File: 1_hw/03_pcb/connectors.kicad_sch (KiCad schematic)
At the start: 0 parts

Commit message: FEAT: Added FTDI JTAG. Added 0 Ohm JTAG Resistors. Added Boot Select Switches.
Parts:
- added R? (x8): 0, Resistor_SMD:R_0603_1608Metric, symbol Device:R_Small
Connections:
- new net JTAG_CON_TCK_3P3: R?.2
- new net JTAG_CON_TDI_3P3: R?.2
- new net JTAG_CON_TDO_3P3: R?.2
- new net JTAG_CON_TMS_3P3: R?.2
- new net JTAG_FTDI_TCK_3P3: R?.2
- new net JTAG_FTDI_TDI_3P3: R?.2
- new net JTAG_FTDI_TDO_3P3: R?.2
- new net JTAG_FTDI_TMS_3P3: R?.2
- new net JTAG_MCU_TCK_3P3: R?.1, R?.1
- new net JTAG_MCU_TDI_3P3: R?.1, R?.1
- new net JTAG_MCU_TDO_3P3: R?.1, R?.1
- new net JTAG_MCU_TMS_3P3: R?.1, R?.1
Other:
- note added: "JTAG 0 OHM CONNECTIONS"

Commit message: FEAT: Simulated Analog Paths, added first stage analog amp to schematic.
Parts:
- R? (x8): symbol Device:R_Small -> Device:R_Small_US
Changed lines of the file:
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@@
 		(rev "0.0.1")
 		(company "Tomasz Brzyzek")
-		(comment 1 "Stasia Brzyzek")
 	)
 	(junction
@@
 	)
 	(symbol
-		(lib_id "Device:R_Small")
+		(lib_id "Device:R_Small_US")
 		(at 229.87 130.81 270)
 		(unit 1)
@@
 			)
 		)
-		(property "Description" ""
+		(property "Description" "Resistor, small US symbol"
 			(at 229.87 130.81 0)
 			(effects
@@
 	)
 	(symbol
-		(lib_id "Device:R_Small")
+		(lib_id "Device:R_Small_US")
 		(at 229.87 111.76 270)
 		(unit 1)
@@
 			)
 		)
-		(property "Description" ""
+		(property "Description" "Resistor, small US symbol"
 			(at 229.87 111.76 0)
 			(effects
@@
 	)
 	(symbol
-		(lib_id "Device:R_Small")
+		(lib_id "Device:R_Small_US")
 		(at 229.87 142.24 270)
 		(unit 1)
@@
 			)
 		)
-		(property "Description" ""
+		(property "Description" "Resistor, small US symbol"
 			(at 229.87 142.24 0)
 			(effects
@@
 	)
 	(symbol
-		(lib_id "Device:R_Small")
+		(lib_id "Device:R_Small_US")
 		(at 229.87 167.64 270)
 		(unit 1)
@@
 			)
 		)
-		(property "Description" ""
+		(property "Description" "Resistor, small US symbol"
 			(at 229.87 167.64 0)
 			(effects
@@
 	)
 	(symbol
-		(lib_id "Device:R_Small")
+		(lib_id "Device:R_Small_US")
 		(at 229.87 149.86 270)
 		(unit 1)
@@
 			)
 		)
-		(property "Description" ""
+		(property "Description" "Resistor, small US symbol"
 			(at 229.87 149.86 0)
 			(effects
@@
 	)
 	(symbol
-		(lib_id "Device:R_Small")
+		(lib_id "Device:R_Small_US")
 		(at 229.87 160.02 270)
 		(unit 1)
@@
 			)
 		)
-		(property "Description" ""
+		(property "Description" "Resistor, small US symbol"
 			(at 229.87 160.02 0)
 			(effects
@@
 	)
 	(symbol
-		(lib_id "Device:R_Small")
+		(lib_id "Device:R_Small_US")
 		(at 229.87 123.19 270)
 		(unit 1)
@@
 			)
 		)
-		(property "Description" ""
+		(property "Description" "Resistor, small US symbol"
 			(at 229.87 123.19 0)
 			(effects
@@
 	)
 	(symbol
-		(lib_id "Device:R_Small")
+		(lib_id "Device:R_Small_US")
 		(at 229.87 104.14 270)
 		(unit 1)
@@
 			)
 		)
-		(property "Description" ""
+		(property "Description" "Resistor, small US symbol"
 			(at 229.87 104.14 0)
 			(effects

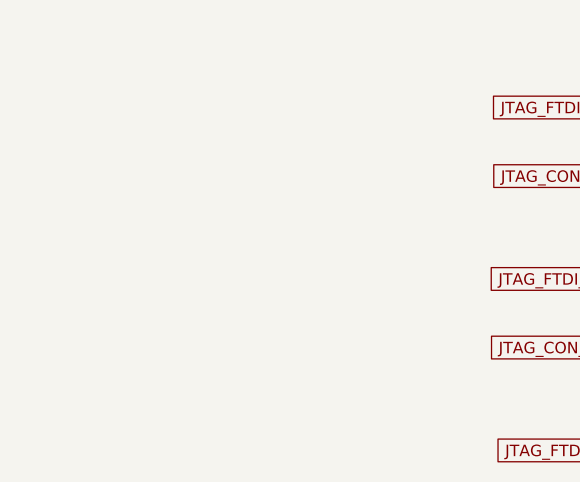
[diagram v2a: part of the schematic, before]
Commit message: FEAT: Added Clocking Sheet, FPGA Flash, and FPGA Decoupling.
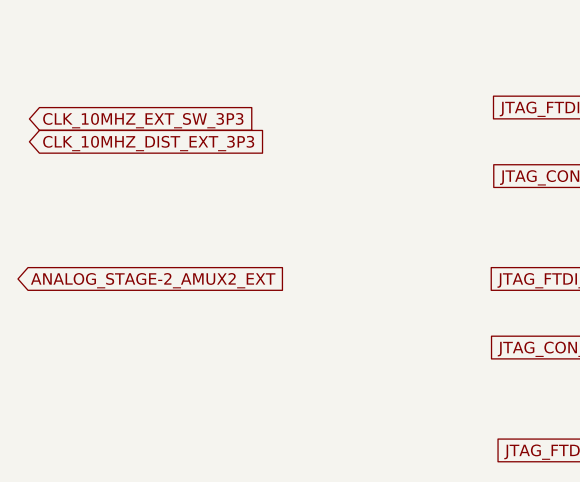
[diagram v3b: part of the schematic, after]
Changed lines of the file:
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@@
+		)
+	)
+	(global_label "ANALOG_STAGE-2_AMUX2_EXT"
+		(shape input)
+		(at 143.51 123.19 0)
+		(fields_autoplaced yes)
+		(effects
+			(font
+				(size 1.27 1.27)
+			)
+			(justify left)
+		)
+		(property "Intersheetrefs" "${INTERSHEET_REFS}"
+			(at 174.6165 123.19 0)
+			(effects
+				(font
+					(size 1.27 1.27)
+				)
+				(justify left)
+				(hide yes)
+			)
 		)
 	)
@@
 		)
 	)
+	(global_label "CLK_10MHZ_EXT_SW_3P3"
+		(shape input)
+		(at 144.78 105.41 0)
+		(fields_autoplaced yes)
+		(effects
+			(font
+				(size 1.27 1.27)
+			)
+			(justify left)
+		)
+		(property "Intersheetrefs" "${INTERSHEET_REFS}"
+			(at 171.2901 105.41 0)
+			(effects
+				(font
+					(size 1.27 1.27)
+				)
+				(justify left)
+				(hide yes)
+			)
+		)
+	)
 	(global_label "JTAG_MCU_TCK_3P3"
 		(shape input)
@@
 			(effects
 				(font
+					(size 1.27 1.27)
+				)
+				(justify left)
+				(hide yes)
+			)
+		)
+	)
+	(global_label "CLK_10MHZ_DIST_EXT_3P3"
+		(shape input)
+		(at 144.78 107.95 0)
+		(fields_autoplaced yes)
+		(effects
+			(font
+				(size 1.27 1.27)
+			)
+			(justify left)
+		)
+		(property "Intersheetrefs" "${INTERSHEET_REFS}"
+			(at 172.6811 107.95 0)
+			(effects
+				(font

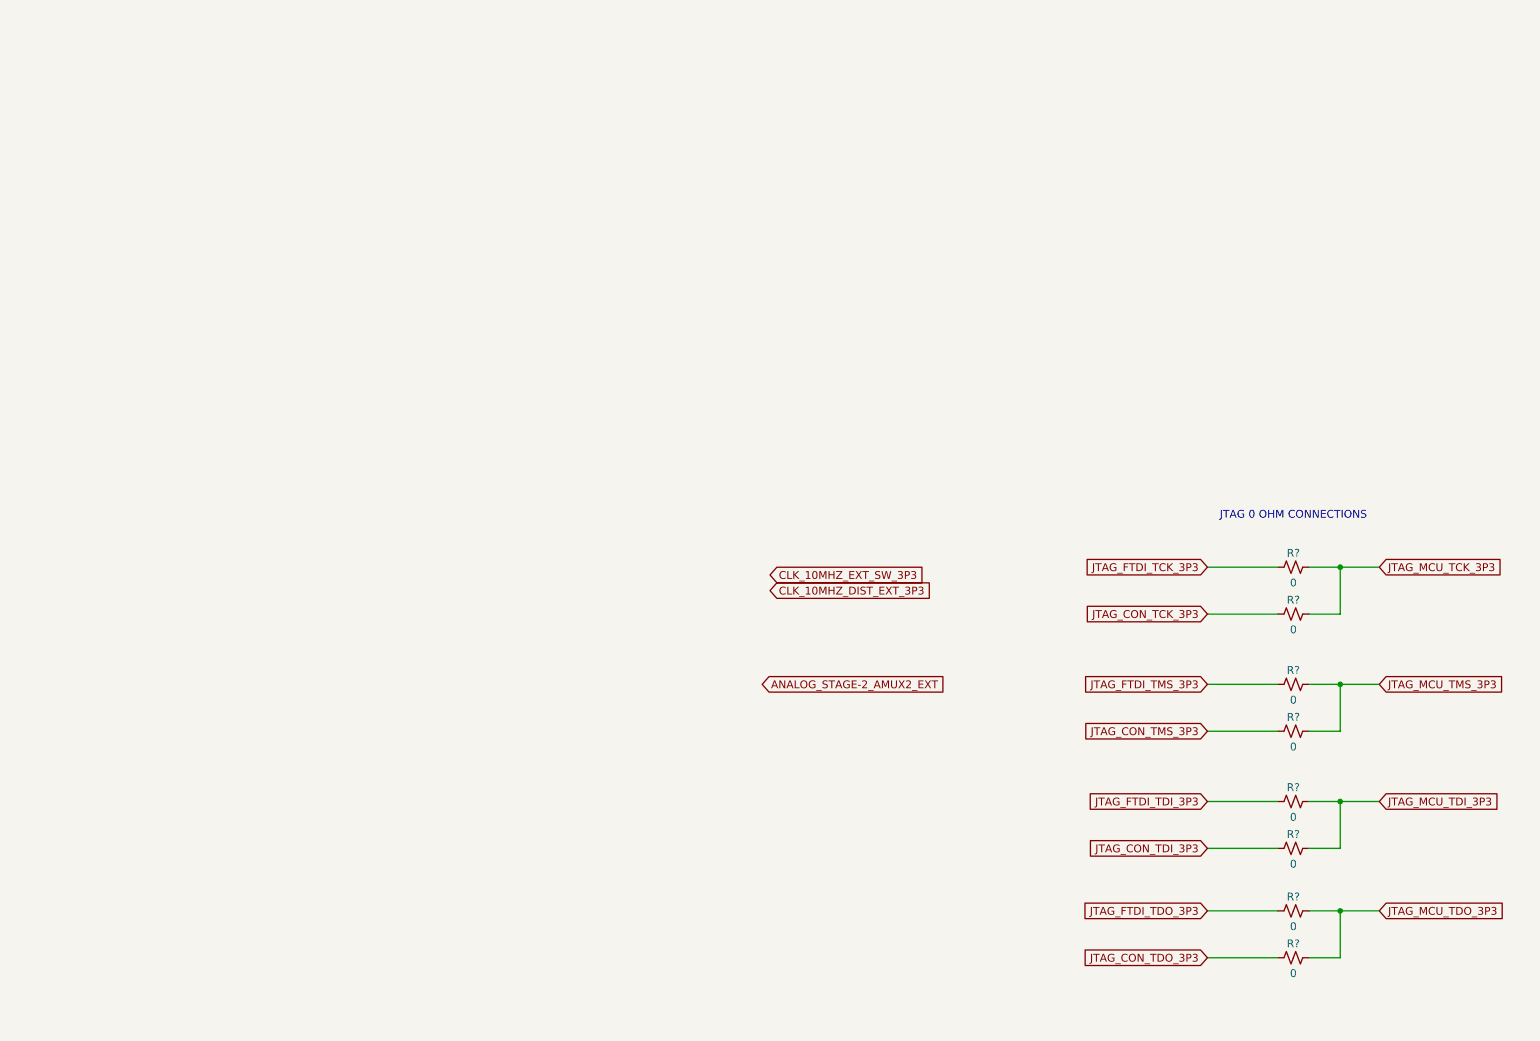
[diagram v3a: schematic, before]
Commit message: FEAT: Added Connectors on Schematic. Created Connector Footprints.
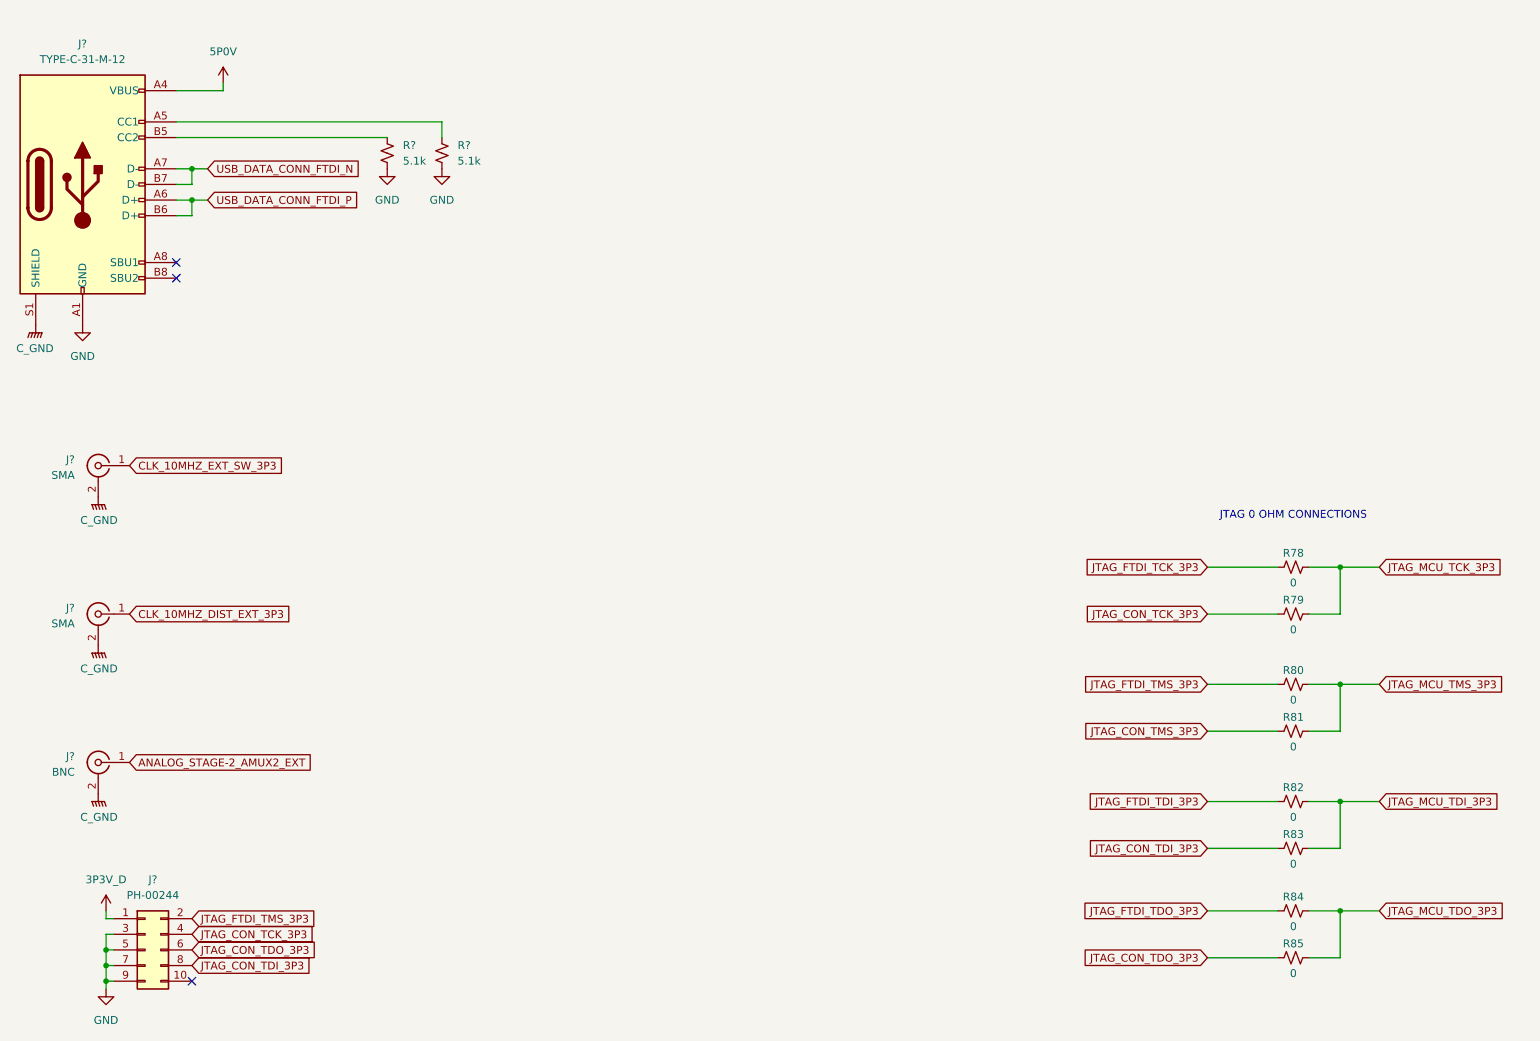
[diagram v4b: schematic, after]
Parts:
- added J?: BNC, BRZK_CONN_COAX:BNC_TH_Horizontal_DOSIN-801-0050, symbol Connector:Conn_Coaxial
- added J?: PH-00244, Connector_PinHeader_2.54mm:PinHeader_2x05_P2.54mm_Vertical, symbol Connector_Generic:Conn_02x05_Odd_Even
- added J? (x2): SMA, BRZK_CONN_COAX:SMA_TH_Horizontal_KH-SMA-K513-G, symbol Connector:Conn_Coaxial
- added J?: TYPE-C-31-M-12, Connector_USB:USB_C_Receptacle_GCT_USB4105-xx-A_16P_TopMnt_Horizontal, symbol BRZK_CONN_USB:TYPE-C-31-M-12
- added R? (x2): 5.1k, Resistor_SMD:R_0603_1608Metric, symbol Device:R_Small_US
- gave numbers to parts that had none: 8
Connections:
- net ANALOG_STAGE-2_AMUX2_EXT: now also J?.1 (In)
- net CLK_10MHZ_DIST_EXT_3P3: now also J?.1 (In)
- net CLK_10MHZ_EXT_SW_3P3: now also J?.1 (In)
- net JTAG_CON_TCK_3P3: now also J?.4 (Pin_4)
- net JTAG_CON_TDI_3P3: now also J?.8 (Pin_8)
- net JTAG_CON_TDO_3P3: now also J?.6 (Pin_6)
- net JTAG_FTDI_TMS_3P3: now also J?.2 (Pin_2)
- new net: J?.A5 (CC1), R?.2
- new net: J?.B5 (CC2), R?.2
- new net 3P3V_D: J?.1 (Pin_1)
- new net 5P0V: J?.A4 (VBUS), J?.A9 (VBUS), J?.B4 (VBUS), J?.B9 (VBUS)
- new net C_GND: J?.2 (Ext), J?.2 (Ext), J?.2 (Ext), J?.S1 (SHIELD)
- new net GND: J?.3 (Pin_3), J?.5 (Pin_5), J?.7 (Pin_7), J?.9 (Pin_9), J?.A1 (GND), J?.A12 (GND), J?.B1 (GND), J?.B12 (GND), R?.1, R?.1
- new net USB_DATA_CONN_FTDI_N: J?.A7 (D-), J?.B7 (D-)
- new net USB_DATA_CONN_FTDI_P: J?.A6 (D+), J?.B6 (D+)
- no-connect marks 0 -> 3

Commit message: FEAT: Assigned Reference Designators; Assigned Passives Part Numbers & Footprints (0603); Assigned LCSC P/Ns.
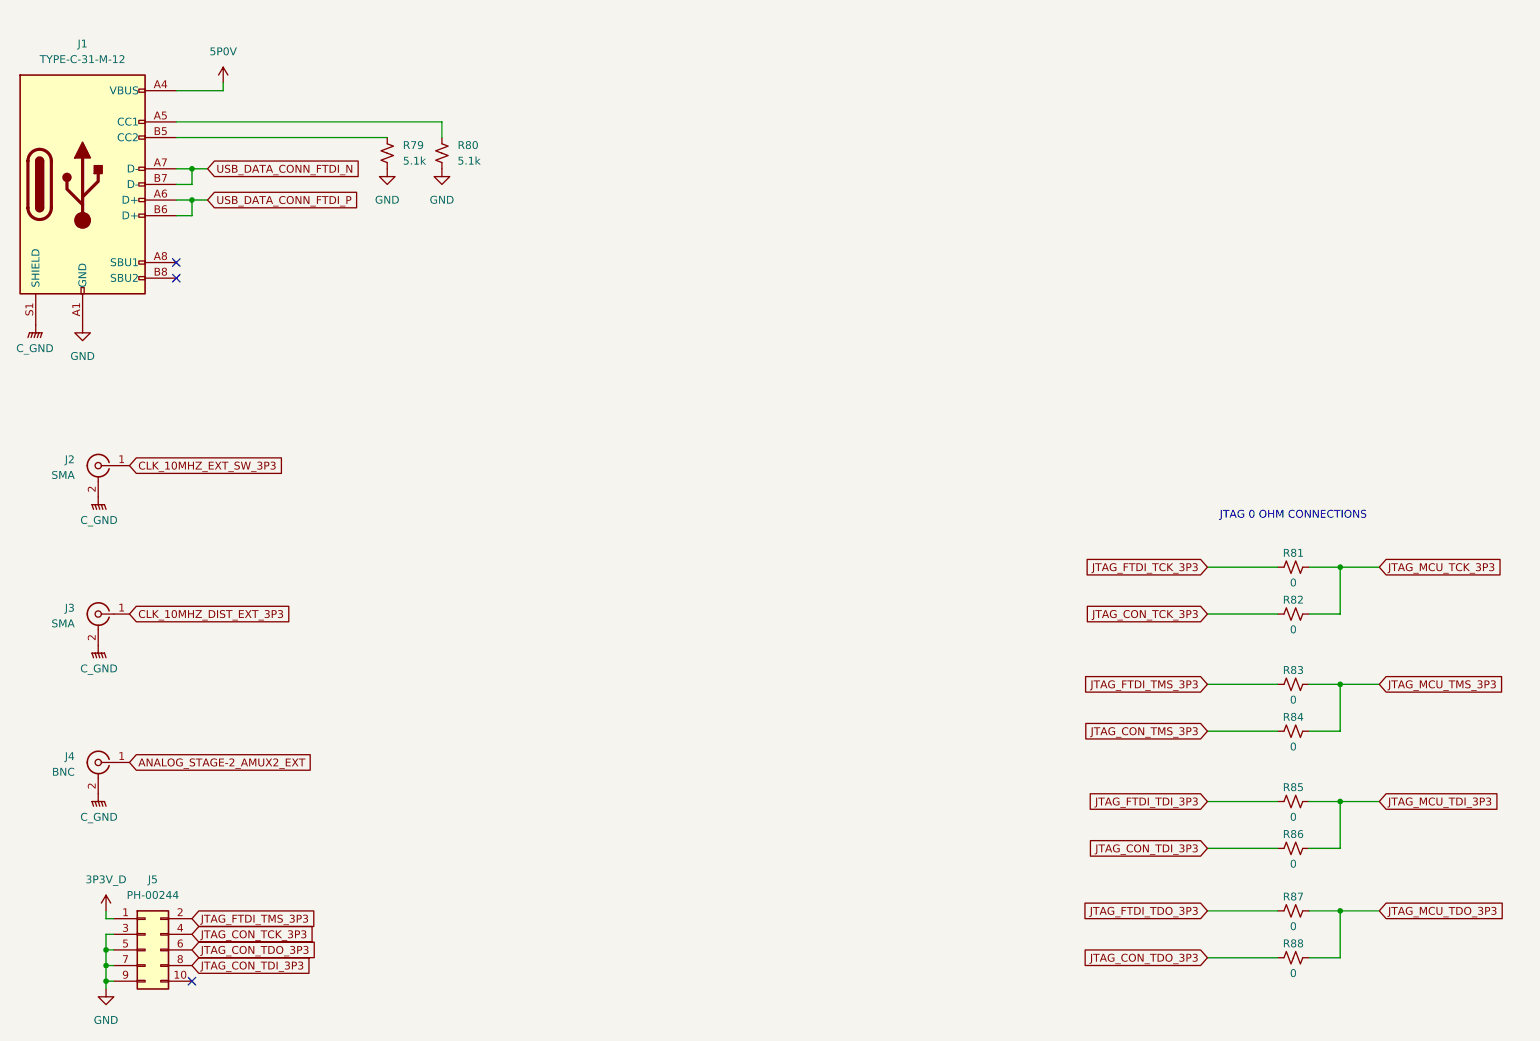
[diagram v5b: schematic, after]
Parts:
- removed R79, R81: 0, Resistor_SMD:R_0603_1608Metric, symbol Device:R_Small_US
- removed R?: 5.1k, Resistor_SMD:R_0603_1608Metric, symbol Device:R_Small_US
- added R86, R87, R88: 0, Resistor_SMD:R_0603_1608Metric, symbol Device:R_Small_US
- J1: renamed from J?; LCSC (none) -> C165948
- J2, J3: renamed from J?; LCSC (none) -> C411575
- J4: renamed from J?; LCSC (none) -> C521210
- J5: renamed from J?; LCSC (none) -> C2829881
- R79: renamed from R?; LCSC (none) -> C23186; Part Number (none) -> 0603WAF5101T5E
- R80: value 0 -> 5.1k; LCSC (none) -> C23186; PN 0603WAJ0000T5E -> (none); Part Number (none) -> 0603WAF5101T5E
- R81: renamed from R78; LCSC (none) -> C15402; PN 0603WAJ0000T5E -> (none); Part Number (none) -> 0603WAJ0000T5E
- R82, R83, R84, R85: LCSC (none) -> C15402; PN 0603WAJ0000T5E -> (none); Part Number (none) -> 0603WAJ0000T5E
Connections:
- net GND: now also R80.1
- net JTAG_CON_TCK_3P3: now also R82.2
- net JTAG_CON_TDI_3P3: now also R86.2; no longer R83.2
- net JTAG_CON_TDO_3P3: now also R88.2; no longer R85.2
- net JTAG_CON_TMS_3P3: now also R84.2
- net JTAG_FTDI_TDI_3P3: now also R85.2; no longer R82.2
- net JTAG_FTDI_TDO_3P3: now also R87.2; no longer R84.2
- net JTAG_FTDI_TMS_3P3: now also R83.2; no longer R80.2
- net JTAG_MCU_TCK_3P3: now also R82.1
- net JTAG_MCU_TDI_3P3: now also R85.1, R86.1; no longer R82.1, R83.1
- net JTAG_MCU_TDO_3P3: now also R87.1, R88.1; no longer R84.1, R85.1
- net JTAG_MCU_TMS_3P3: now also R83.1, R84.1; no longer R80.1
- net at J1.A5 (CC1): now also R80.2
